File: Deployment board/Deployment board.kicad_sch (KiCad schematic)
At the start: 0 parts

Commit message: finished sensors except gps
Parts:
- added C33: 1000u, symbol Device:C
- added C34: 100n, symbol Device:C
- added D10: TVS, symbol Device:D_TVS_Filled
- added D4, D5: D_Schottky, symbol Device:D_Schottky
- added D6, D7: LED, symbol Device:LED
- added D9: B_3V3, symbol Device:LED
- added F3: Fuse (>15A), symbol Device:Fuse
- added GND1, V_D_BAT+: TestPoint, symbol Connector:TestPoint
- added J11, J9: Conn_01x04, symbol Connector_Generic:Conn_01x04
- added J5, J7, J8: Conn_01x02, symbol Connector_Generic:Conn_01x02
- added M1: Motor_Servo, symbol Motor:Motor_Servo
- added Q3, Q4: IRLR7843, symbol Simulation_SPICE:NMOS
- added Q6: To be determined, Package_TO_SOT_SMD:SOT-23, symbol Transistor_FET:IRLML6402
- added R30, R31, R32, R36: 1k, symbol Device:R
- added R33, R34: 3.3k, symbol Device:R
- added R37: 100k, symbol Device:R
- added SW1: REMOVE BEFORE FLIGHT, symbol Switch:SW_SPST
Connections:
- new net: D4.1 (K), D5.1 (K), M1.1 (PWM), R30.1
- new net: D7.2 (A), J7.1 (Pin_1), Q3.1 (D)
- new net: D7.1 (K), R34.1
- new net: Q6.2 (S), SW1.1 (A)
- new net: Q6.1 (G), R37.1
- new net: D10.2 (A2), F3.2, Q6.3 (D)
- new net: D6.1 (K), R33.1
- new net: F3.1, J5.1 (Pin_1)
- new net: D6.2 (A), J8.1 (Pin_1), Q4.1 (D)
- new net: D9.2 (A), R36.1
- new net Backup_AV_FIRE: J9.2 (Pin_2), Q4.2 (G), R32.1
- new net Backup_AV_PWM_Servo: D5.2 (A), J9.1 (Pin_1)
- new net GND: C33.2, C34.2, D10.1 (A1), D9.1 (K), GND1.1, J11.3 (Pin_3), J11.4 (Pin_4), J5.2 (Pin_2), J9.3 (Pin_3), J9.4 (Pin_4), M1.3 (-), Q3.3 (S), Q4.3 (S), R30.2, R31.2, R32.2, R33.2, R34.2, R37.2
- new net Main_AV_FIRE: J11.2 (Pin_2), Q3.2 (G), R31.1
- new net Main_AV_PWM_Servo: D4.2 (A), J11.1 (Pin_1)
- new net V_D_BAT+: R36.2, SW1.2 (B), V_D_BAT+.1
- new net V_Ｄ_BAT+: C33.1, C34.1, J7.2 (Pin_2), J8.2 (Pin_2), M1.2 (+)
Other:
- note added: "1k pull down for lower time constant(tau=RC)"
- note added: "Connectors"
- note added: "Heat Wire(for main parachute deployment)"
- note added: "Indicator"
- note added: "Reverse Protection & Remove Before Flight"
- note added: "Servo(for drogue parachute deployment)"
- note added: "Test point"
- note added: "connect to hot wire"

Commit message: add some package of Deployment board
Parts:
- C1: renamed from C34; footprint (none) -> Capacitor_SMD:C_0805_2012Metric_Pad1.18x1.45mm_HandSolder
- C2: renamed from C33; footprint (none) -> Capacitor_THT:C_Radial_D10.0mm_H20.0mm_P5.00mm
- D1: renamed from D4; footprint (none) -> Diode_SMD:D_0805_2012Metric_Pad1.15x1.40mm_HandSolder
- D2: renamed from D5; footprint (none) -> Diode_SMD:D_0805_2012Metric_Pad1.15x1.40mm_HandSolder
- D3: renamed from D7; footprint (none) -> LED_SMD:LED_1206_3216Metric_Pad1.42x1.75mm_HandSolder
- D4: renamed from D6; footprint (none) -> LED_SMD:LED_1206_3216Metric_Pad1.42x1.75mm_HandSolder
- D5: renamed from D10; footprint (none) -> Diode_SMD:D_SMA-SMB_Universal_Handsoldering
- D6: renamed from D9; footprint (none) -> LED_SMD:LED_1206_3216Metric_Pad1.42x1.75mm_HandSolder
- F1: renamed from F3; footprint (none) -> Fuse:Fuse_0603_1608Metric_Pad1.05x0.95mm_HandSolder
- GND1: footprint (none) -> TestPoint:TestPoint_THTPad_D1.5mm_Drill0.7mm
- J1: renamed from J11; footprint (none) -> Connector_PinSocket_2.54mm:PinSocket_1x04_P2.54mm_Horizontal
- J2: renamed from J9; footprint (none) -> Connector_PinSocket_2.54mm:PinSocket_1x04_P2.54mm_Horizontal
- J3: renamed from J7; footprint (none) -> Connector_PinSocket_2.54mm:PinSocket_1x02_P2.54mm_Horizontal
- J4: renamed from J8; footprint (none) -> Connector_PinSocket_2.54mm:PinSocket_1x02_P2.54mm_Horizontal
- J5: footprint (none) -> Connector_PinHeader_2.54mm:PinHeader_1x02_P2.54mm_Vertical
- M1: footprint (none) -> Connector_PinHeader_2.54mm:PinHeader_1x03_P2.54mm_Horizontal
- Q1: renamed from Q3; footprint (none) -> Package_TO_SOT_SMD:TO-252-2
- Q2: renamed from Q4; footprint (none) -> Package_TO_SOT_SMD:TO-252-2
- R1: renamed from R31; footprint (none) -> Resistor_SMD:R_0805_2012Metric_Pad1.20x1.40mm_HandSolder
- R2: renamed from R32; footprint (none) -> Resistor_SMD:R_0805_2012Metric_Pad1.20x1.40mm_HandSolder
- R3: renamed from R30; footprint (none) -> Resistor_SMD:R_0805_2012Metric_Pad1.20x1.40mm_HandSolder
- R4: renamed from R34; footprint (none) -> Resistor_SMD:R_0805_2012Metric_Pad1.20x1.40mm_HandSolder
- R5: renamed from R33; footprint (none) -> Resistor_SMD:R_0805_2012Metric_Pad1.20x1.40mm_HandSolder
- R6: renamed from R37; footprint (none) -> Resistor_SMD:R_0805_2012Metric_Pad1.20x1.40mm_HandSolder
- R7: renamed from R36; footprint (none) -> Resistor_SMD:R_0805_2012Metric_Pad1.20x1.40mm_HandSolder
- V_D_BAT+1: renamed from V_D_BAT+; footprint (none) -> TestPoint:TestPoint_THTPad_D1.5mm_Drill0.7mm
- renumbered Q6 to Q3
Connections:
- net V_Ｄ_BAT+: no longer J3.2 (Pin_2)

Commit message: some changes on Deployment board pcb
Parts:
- C2: footprint Capacitor_THT:C_Radial_D10.0mm_H20.0mm_P5.00mm -> Capacitor_THT:C_Radial_D8.0mm_H7.0mm_P3.50mm
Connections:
- net V_Ｄ_BAT+: now also J3.1 (Pin_1)
- net at D3.2 (A), Q1.1 (D): now also J3.2 (Pin_2); no longer J3.1 (Pin_1)
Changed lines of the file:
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@@
 	(wire
 		(pts
-			(xy 93.98 88.9) (xy 93.98 91.44)
+			(xy 97.79 86.36) (xy 97.79 88.9)
 		)
 		(stroke
@@
 	(wire
 		(pts
-			(xy 97.79 78.74) (xy 97.79 86.36)
+			(xy 66.04 111.76) (xy 66.04 114.3)
 		)
 		(stroke
@@
 	(wire
 		(pts
-			(xy 66.04 111.76) (xy 66.04 114.3)
+			(xy 97.79 78.74) (xy 97.79 83.82)
 		)
 		(stroke
@@
 	(wire
 		(pts
-			(xy 93.98 88.9) (xy 97.79 88.9)
-		)
-		(stroke
-			(width 0)
-			(type default)
-		)
-	)
-	(wire
-		(pts
 			(xy 43.18 31.75) (xy 52.07 31.75)
 		)
@@
 			)
 		)
-		(property "Footprint" "Capacitor_THT:C_Radial_D10.0mm_H20.0mm_P5.00mm"
+		(property "Footprint" "Capacitor_THT:C_Radial_D8.0mm_H7.0mm_P3.50mm"
 			(at 59.9948 52.07 0)
 			(effects
@@
 	(symbol
 		(lib_id "power:VAA")
-		(at 93.98 91.44 180)
+		(at 97.79 88.9 180)
 		(unit 1)
 		(exclude_from_sim no)
@@
 		(dnp no)
 		(property "Reference" "#PWR010"
-			(at 93.98 87.63 0)
+			(at 97.79 85.09 0)
 			(effects
 				(font
@@
 		)
 		(property "Value" "V_Ｄ_BAT+"
-			(at 99.06 96.52 0)
+			(at 102.87 93.98 0)
 			(effects
 				(font
@@
 		)
 		(property "Footprint" ""
-			(at 93.98 91.44 0)
+			(at 97.79 88.9 0)
 			(effects
 				(font
@@
 		)
 		(property "Datasheet" ""
-			(at 93.98 91.44 0)
+			(at 97.79 88.9 0)
 			(effects
 				(font
@@
 		)
 		(property "Description" "Power symbol creates a global label with name \"VAA\""
-			(at 93.98 91.44 0)
+			(at 97.79 88.9 0)
 			(effects
 				(font

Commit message: update Deployment board
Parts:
- J5: footprint Connector_PinHeader_2.54mm:PinHeader_1x02_P2.54mm_Vertical -> Connector_PinHeader_2.54mm:PinHeader_1x02_P2.54mm_Horizontal
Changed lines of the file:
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@@
 			)
 		)
-		(property "Footprint" "Connector_PinHeader_2.54mm:PinHeader_1x02_P2.54mm_Vertical"
+		(property "Footprint" "Connector_PinHeader_2.54mm:PinHeader_1x02_P2.54mm_Horizontal"
 			(at 130.81 30.48 0)
 			(effects

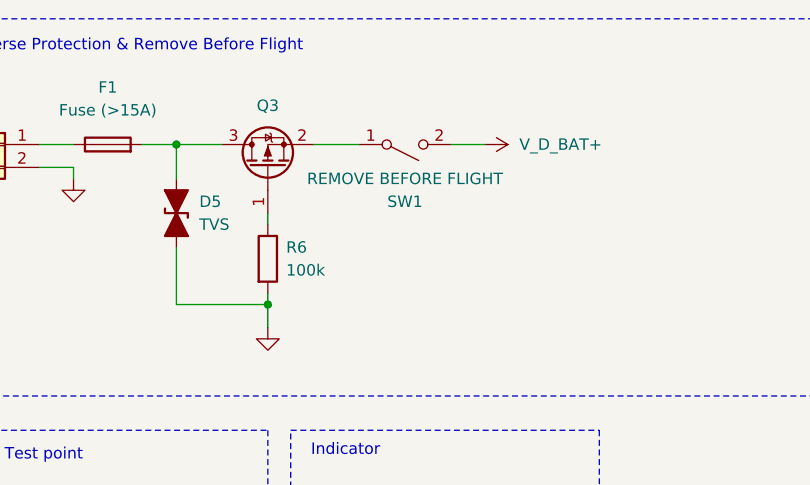
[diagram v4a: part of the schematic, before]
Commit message: add hole to connect wire
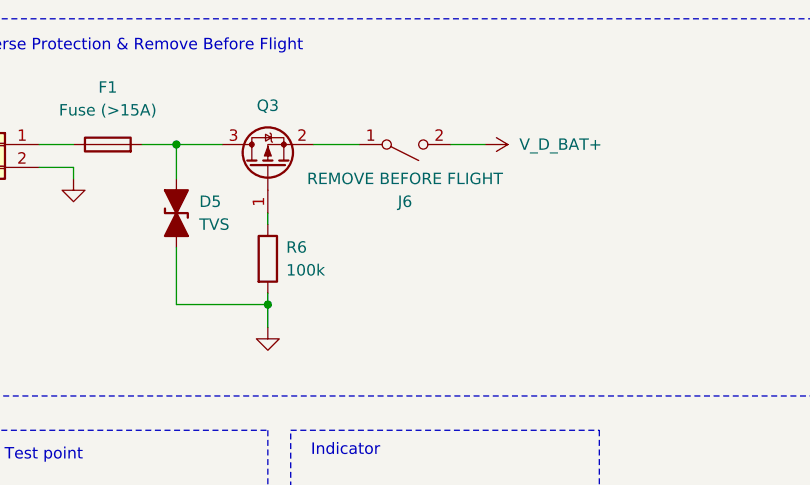
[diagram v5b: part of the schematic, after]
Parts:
- J5: footprint Connector_PinHeader_2.54mm:PinHeader_1x02_P2.54mm_Horizontal -> Connector_Wire:SolderWire-2sqmm_1x02_P7.8mm_D2mm_OD3.9mm
- J6: renamed from SW1; footprint (none) -> Connector_Wire:SolderWire-2sqmm_1x02_P7.8mm_D2mm_OD3.9mm
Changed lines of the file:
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@@
 		(on_board yes)
 		(dnp no)
-		(property "Reference" "SW1"
+		(property "Reference" "J6"
 			(at 176.53 36.83 0)
 			(effects
@@
 			)
 		)
-		(property "Footprint" ""
+		(property "Footprint" "Connector_Wire:SolderWire-2sqmm_1x02_P7.8mm_D2mm_OD3.9mm"
 			(at 176.53 30.48 0)
 			(effects
@@
 			(project ""
 				(path "/0306e6d1-d01c-48b9-a21d-45e3980b499b"
-					(reference "SW1")
+					(reference "J6")
 					(unit 1)
 				)
@@
 		(on_board yes)
 		(dnp no)
-		(property "Reference" "#PWR011"
+		(property "Reference" "#PWR010"
 			(at 93.98 106.68 0)
 			(effects
@@
 			(project "Deployment board"
 				(path "/0306e6d1-d01c-48b9-a21d-45e3980b499b"
-					(reference "#PWR011")
+					(reference "#PWR010")
 					(unit 1)
 				)
@@
 		(on_board yes)
 		(dnp no)
-		(property "Reference" "#PWR010"
+		(property "Reference" "#PWR011"
 			(at 97.79 85.09 0)
 			(effects
@@
 			(project "Deployment board"
 				(path "/0306e6d1-d01c-48b9-a21d-45e3980b499b"
-					(reference "#PWR010")
+					(reference "#PWR011")
 					(unit 1)
 				)
@@
 			)
 		)
-		(property "Footprint" "Connector_PinHeader_2.54mm:PinHeader_1x02_P2.54mm_Horizontal"
+		(property "Footprint" "Connector_Wire:SolderWire-2sqmm_1x02_P7.8mm_D2mm_OD3.9mm"
 			(at 130.81 30.48 0)
 			(effects

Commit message: jpush
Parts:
- J1, J2: footprint Connector_PinSocket_2.54mm:PinSocket_1x04_P2.54mm_Horizontal -> Connector_PinSocket_2.54mm:PinSocket_1x04_P2.54mm_Vertical
- J3, J4: footprint Connector_PinSocket_2.54mm:PinSocket_1x02_P2.54mm_Horizontal -> Connector_PinSocket_2.54mm:PinSocket_1x02_P2.54mm_Vertical
- J5: footprint Connector_Wire:SolderWire-2sqmm_1x02_P7.8mm_D2mm_OD3.9mm -> Connector_JST:JST_EH_B2B-EH-A_1x02_P2.50mm_Vertical
- J6: footprint Connector_Wire:SolderWire-2sqmm_1x02_P7.8mm_D2mm_OD3.9mm -> Button_Switch_THT:SW_NKK_G1xJP
- M1: footprint Connector_PinHeader_2.54mm:PinHeader_1x03_P2.54mm_Horizontal -> Connector_PinHeader_2.54mm:PinHeader_1x03_P2.54mm_Vertical
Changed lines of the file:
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@@
 			)
 		)
-		(property "Footprint" "Connector_PinHeader_2.54mm:PinHeader_1x03_P2.54mm_Horizontal"
+		(property "Footprint" "Connector_PinHeader_2.54mm:PinHeader_1x03_P2.54mm_Vertical"
 			(at 74.93 49.276 0)
 			(effects
@@
 			)
 		)
-		(property "Footprint" "Connector_Wire:SolderWire-2sqmm_1x02_P7.8mm_D2mm_OD3.9mm"
+		(property "Footprint" "Button_Switch_THT:SW_NKK_G1xJP"
 			(at 176.53 30.48 0)
 			(effects
@@
 			)
 		)
-		(property "Footprint" "Connector_PinSocket_2.54mm:PinSocket_1x02_P2.54mm_Horizontal"
+		(property "Footprint" "Connector_PinSocket_2.54mm:PinSocket_1x02_P2.54mm_Vertical"
 			(at 102.87 86.36 0)
 			(effects
@@
 			)
 		)
-		(property "Footprint" "Connector_PinSocket_2.54mm:PinSocket_1x04_P2.54mm_Horizontal"
+		(property "Footprint" "Connector_PinSocket_2.54mm:PinSocket_1x04_P2.54mm_Vertical"
 			(at 71.12 144.78 0)
 			(effects
@@
 		)
 		(property "Value" "TVS"
-			(at 153.67 39.3699 90)
+			(at 153.67 38.862 90)
 			(effects
 				(font
@@
 			)
 		)
-		(property "Footprint" "Connector_PinSocket_2.54mm:PinSocket_1x02_P2.54mm_Horizontal"
+		(property "Footprint" "Connector_PinSocket_2.54mm:PinSocket_1x02_P2.54mm_Vertical"
 			(at 102.87 106.68 0)
 			(effects
@@
 			)
 		)
-		(property "Footprint" "Connector_Wire:SolderWire-2sqmm_1x02_P7.8mm_D2mm_OD3.9mm"
+		(property "Footprint" "Connector_JST:JST_EH_B2B-EH-A_1x02_P2.50mm_Vertical"
 			(at 130.81 30.48 0)
 			(effects
@@
 			)
 		)
-		(property "Footprint" "Connector_PinSocket_2.54mm:PinSocket_1x04_P2.54mm_Horizontal"
+		(property "Footprint" "Connector_PinSocket_2.54mm:PinSocket_1x04_P2.54mm_Vertical"
 			(at 25.4 144.78 0)
 			(effects

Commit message: jpush
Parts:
- J1, J2: footprint Connector_PinSocket_2.54mm:PinSocket_1x04_P2.54mm_Vertical -> Connector_PinSocket_2.54mm:PinSocket_1x04_P2.54mm_Horizontal
- J3, J4: footprint Connector_PinSocket_2.54mm:PinSocket_1x02_P2.54mm_Vertical -> Connector_PinSocket_2.54mm:PinSocket_1x02_P2.54mm_Horizontal
- J5: footprint Connector_JST:JST_EH_B2B-EH-A_1x02_P2.50mm_Vertical -> Connector_Wire:SolderWire-2sqmm_1x02_P7.8mm_D2mm_OD3.9mm
- J6: footprint Button_Switch_THT:SW_NKK_G1xJP -> Connector_Wire:SolderWire-2sqmm_1x02_P7.8mm_D2mm_OD3.9mm
- M1: footprint Connector_PinHeader_2.54mm:PinHeader_1x03_P2.54mm_Vertical -> Connector_PinHeader_2.54mm:PinHeader_1x03_P2.54mm_Horizontal
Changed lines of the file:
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@@
 			)
 		)
-		(property "Footprint" "Connector_PinHeader_2.54mm:PinHeader_1x03_P2.54mm_Vertical"
+		(property "Footprint" "Connector_PinHeader_2.54mm:PinHeader_1x03_P2.54mm_Horizontal"
 			(at 74.93 49.276 0)
 			(effects
@@
 			)
 		)
-		(property "Footprint" "Button_Switch_THT:SW_NKK_G1xJP"
+		(property "Footprint" "Connector_Wire:SolderWire-2sqmm_1x02_P7.8mm_D2mm_OD3.9mm"
 			(at 176.53 30.48 0)
 			(effects
@@
 			)
 		)
-		(property "Footprint" "Connector_PinSocket_2.54mm:PinSocket_1x02_P2.54mm_Vertical"
+		(property "Footprint" "Connector_PinSocket_2.54mm:PinSocket_1x02_P2.54mm_Horizontal"
 			(at 102.87 86.36 0)
 			(effects
@@
 			)
 		)
-		(property "Footprint" "Connector_PinSocket_2.54mm:PinSocket_1x04_P2.54mm_Vertical"
+		(property "Footprint" "Connector_PinSocket_2.54mm:PinSocket_1x04_P2.54mm_Horizontal"
 			(at 71.12 144.78 0)
 			(effects
@@
 		)
 		(property "Value" "TVS"
-			(at 153.67 38.862 90)
+			(at 153.67 39.3699 90)
 			(effects
 				(font
@@
 			)
 		)
-		(property "Footprint" "Connector_PinSocket_2.54mm:PinSocket_1x02_P2.54mm_Vertical"
+		(property "Footprint" "Connector_PinSocket_2.54mm:PinSocket_1x02_P2.54mm_Horizontal"
 			(at 102.87 106.68 0)
 			(effects
@@
 			)
 		)
-		(property "Footprint" "Connector_JST:JST_EH_B2B-EH-A_1x02_P2.50mm_Vertical"
+		(property "Footprint" "Connector_Wire:SolderWire-2sqmm_1x02_P7.8mm_D2mm_OD3.9mm"
 			(at 130.81 30.48 0)
 			(effects
@@
 			)
 		)
-		(property "Footprint" "Connector_PinSocket_2.54mm:PinSocket_1x04_P2.54mm_Vertical"
+		(property "Footprint" "Connector_PinSocket_2.54mm:PinSocket_1x04_P2.54mm_Horizontal"
 			(at 25.4 144.78 0)
 			(effects
